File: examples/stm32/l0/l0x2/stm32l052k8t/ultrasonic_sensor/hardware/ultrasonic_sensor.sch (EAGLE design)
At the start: 31 parts, among them IC1 MCP1702T-3302E/TO, M1 STM32L052K8T_DIP, M2 HC-SR04, Q1 NDS332P, Q2 NDS332P, Q3 NDS332P, Q4 NDS332P

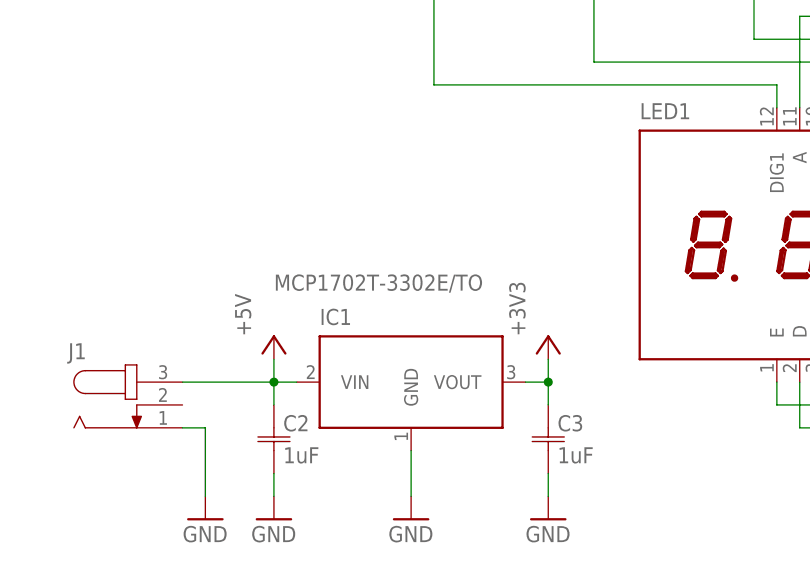
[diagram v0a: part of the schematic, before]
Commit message: Fix ultrasonic_sensor.
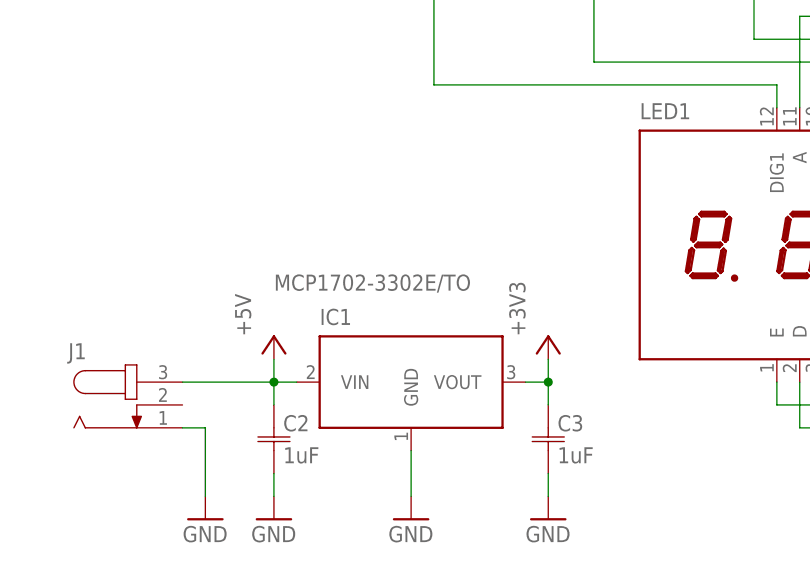
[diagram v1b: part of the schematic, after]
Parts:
- IC1: value MCP1702T-3302E/TO -> MCP1702-3302E/TO; device v-reg:MCP1702T-3302E/TO -> v-reg:MCP1702-3302E/TO
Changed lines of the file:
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@@
 <?xml version="1.0" encoding="utf-8"?>
 <!DOCTYPE eagle SYSTEM "eagle.dtd">
-<eagle version="7.7.0">
+<eagle version="8.3.0">
 <drawing>
 <settings>
 <setting alwaysvectorfont="no"/>
+<setting keepoldvectorfont="yes"/>
 <setting verticaltext="up"/>
 </settings>
-<grid distance="0.1" unitdist="inch" unit="inch" style="lines" multiple="1" display="yes" altdistance="0.01" altunitdist="inch" altunit="inch"/>
+<grid distance="0.1" unitdist="inch" unit="inch" style="lines" multiple="1" display="no" altdistance="0.01" altunitdist="inch" altunit="inch"/>
 <layers>
-<layer number="1" name="Top" color="4" fill="1" visible="no" active="no"/>
-<layer number="16" name="Bottom" color="1" fill="1" visible="no" active="no"/>
-<layer number="17" name="Pads" color="2" fill="1" visible="no" active="no"/>
-<layer number="18" name="Vias" color="2" fill="1" visible="no" active="no"/>
-<layer number="19" name="Unrouted" color="6" fill="1" visible="no" active="no"/>
-<layer number="20" name="Dimension" color="15" fill="1" visible="no" active="no"/>
-<layer number="21" name="tPlace" color="7" fill="1" visible="no" active="no"/>
-<layer number="22" name="bPlace" color="7" fill="1" visible="no" active="no"/>
-<layer number="23" name="tOrigins" color="15" fill="1" visible="no" active="no"/>
-<layer number="24" name="bOrigins" color="15" fill="1" visible="no" active="no"/>
-<layer number="25" name="tNames" color="7" fill="1" visible="no" active="no"/>
-<layer number="26" name="bNames" color="7" fill="1" visible="no" active="no"/>
-<layer number="27" name="tValues" color="7" fill="1" visible="no" active="no"/>
-<layer number="28" name="bValues" color="7" fill="1" visible="no" active="no"/>
+<layer number="1" name="Top" color="4" fill="1" visible="yes" active="no"/>
+<layer number="16" name="Bottom" color="1" fill="1" visible="yes" active="no"/>
+<layer number="17" name="Pads" color="2" fill="1" visible="yes" active="no"/>
+<layer number="18" name="Vias" color="2" fill="1" visible="yes" active="no"/>
+<layer number="19" name="Unrouted" color="6" fill="1" visible="yes" active="no"/>
+<layer number="20" name="Dimension" color="15" fill="1" visible="yes" active="no"/>
+<layer number="21" name="tPlace" color="7" fill="1" visible="yes" active="no"/>
+<layer number="22" name="bPlace" color="7" fill="1" visible="yes" active="no"/>
+<layer number="23" name="tOrigins" color="15" fill="1" visible="yes" active="no"/>
+<layer number="24" name="bOrigins" color="15" fill="1" visible="yes" active="no"/>
+<layer number="25" name="tNames" color="7" fill="1" visible="yes" active="no"/>
+<layer number="26" name="bNames" color="7" fill="1" visible="yes" active="no"/>
+<layer number="27" name="tValues" color="7" fill="1" visible="yes" active="no"/>
+<layer number="28" name="bValues" color="7" fill="1" visible="yes" active="no"/>
 <layer number="29" name="tStop" color="7" fill="3" visible="no" active="no"/>
 <layer number="30" name="bStop" color="7" fill="6" visible="no" active="no"/>
@@
 <layer number="35" name="tGlue" color="7" fill="4" visible="no" active="no"/>
 <layer number="36" name="bGlue" color="7" fill="5" visible="no" active="no"/>
-<layer number="37" name="tTest" color="7" fill="1" visible="no" active="no"/>
-<layer number="38" name="bTest" color="7" fill="1" visible="no" active="no"/>
+<layer number="37" name="tTest" color="7" fill="1" visible="yes" active="no"/>
+<layer number="38" name="bTest" color="7" fill="1" visible="yes" active="no"/>
 <layer number="39" name="tKeepout" color="4" fill="11" visible="no" active="no"/>
 <layer number="40" name="bKeepout" color="1" fill="11" visible="no" active="no"/>
@@
 <layer number="44" name="Drills" color="7" fill="1" visible="no" active="no"/>
 <layer number="45" name="Holes" color="7" fill="1" visible="no" active="no"/>
-<layer number="46" name="Milling" color="3" fill="1" visible="no" active="no"/>
-<layer number="47" name="Measures" color="7" fill="1" visible="no" active="no"/>
-<layer number="48" name="Document" color="7" fill="1" visible="no" active="no"/>
-<layer number="49" name="Reference" color="7" fill="1" visible="no" active="no"/>
-<layer number="50" name="dxf" color="7" fill="1" visible="no" active="no"/>
-<layer number="51" name="tDocu" color="7" fill="1" visible="no" active="no"/>
-<layer number="52" name="bDocu" color="7" fill="1" visible="no" active="no"/>
-<layer number="53" name="tGND_GNDA" color="7" fill="9" visible="no" active="no"/>
-<layer number="54" name="bGND_GNDA" color="1" fill="9" visible="no" active="no"/>
-<layer number="56" name="wert" color="7" fill="1" visible="no" active="no"/>
-<layer number="57" name="tCAD" color="7" fill="1" visible="no" active="no"/>
+<layer number="46" name="Milling" color="3" fill="1" visible="yes" active="no"/>
+<layer number="47" name="Measures" color="7" fill="1" visible="yes" active="no"/>
+<layer number="48" name="Document" color="7" fill="1" visible="yes" active="no"/>
+<layer number="49" name="Reference" color="7" fill="1" visible="yes" active="no"/>
+<layer number="50" name="dxf" color="7" fill="1" visible="yes" active="no"/>
+<layer number="51" name="tDocu" color="7" fill="1" visible="yes" active="no"/>
+<layer number="52" name="bDocu" color="7" fill="1" visible="yes" active="no"/>
+<layer number="53" name="tGND_GNDA" color="7" fill="9" visible="yes" active="no"/>
+<layer number="54" name="bGND_GNDA" color="1" fill="9" visible="yes" active="no"/>
+<layer number="56" name="wert" color="7" fill="1" visible="yes" active="no"/>
+<layer number="57" name="tCAD" color="7" fill="1" visible="yes" active="no"/>
 <layer number="90" name="Modules" color="5" fill="1" visible="yes" active="yes"/>
 <layer number="91" name="Nets" color="2" fill="1" visible="yes" active="yes"/>
@@
 <part name="GND2" library="supply1" deviceset="GND" device=""/>
 <part name="J1" library="con-jack" deviceset="JACK-PLUG" device="0"/>
-<part name="IC1" library="v-reg" deviceset="MCP1702" device="TO" technology="T-3302E/"/>
+<part name="IC1" library="v-reg" deviceset="MCP1702" device="TO" technology="-3302E/" value="MCP1702-3302E/TO"/>
 <part name="C2" library="cap" deviceset="C-JIS" device="050-024X044" value="1uF"/>
 <part name="C3" library="cap" deviceset="C-JIS" device="050-024X044" value="1uF"/>
